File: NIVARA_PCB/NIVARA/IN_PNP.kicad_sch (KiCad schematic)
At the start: 0 parts

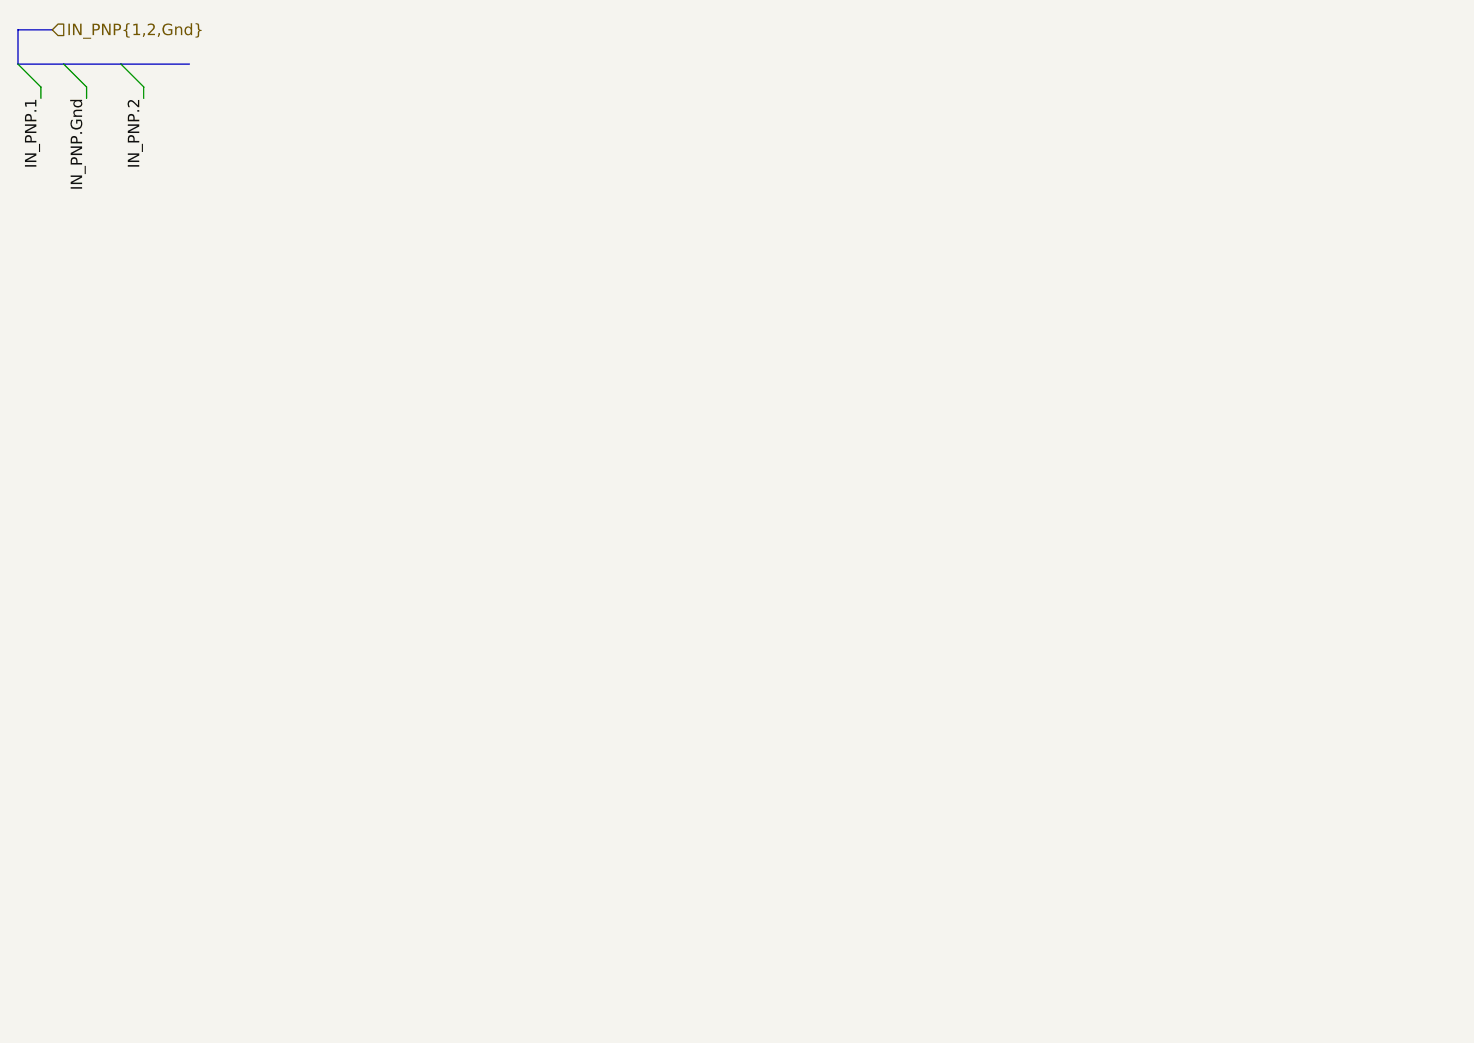
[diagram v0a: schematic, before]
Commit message: AVANCES
se realizaron avances con las entradas NPN, PNP. tambien se realizaron avances con las salidas de RELAYS
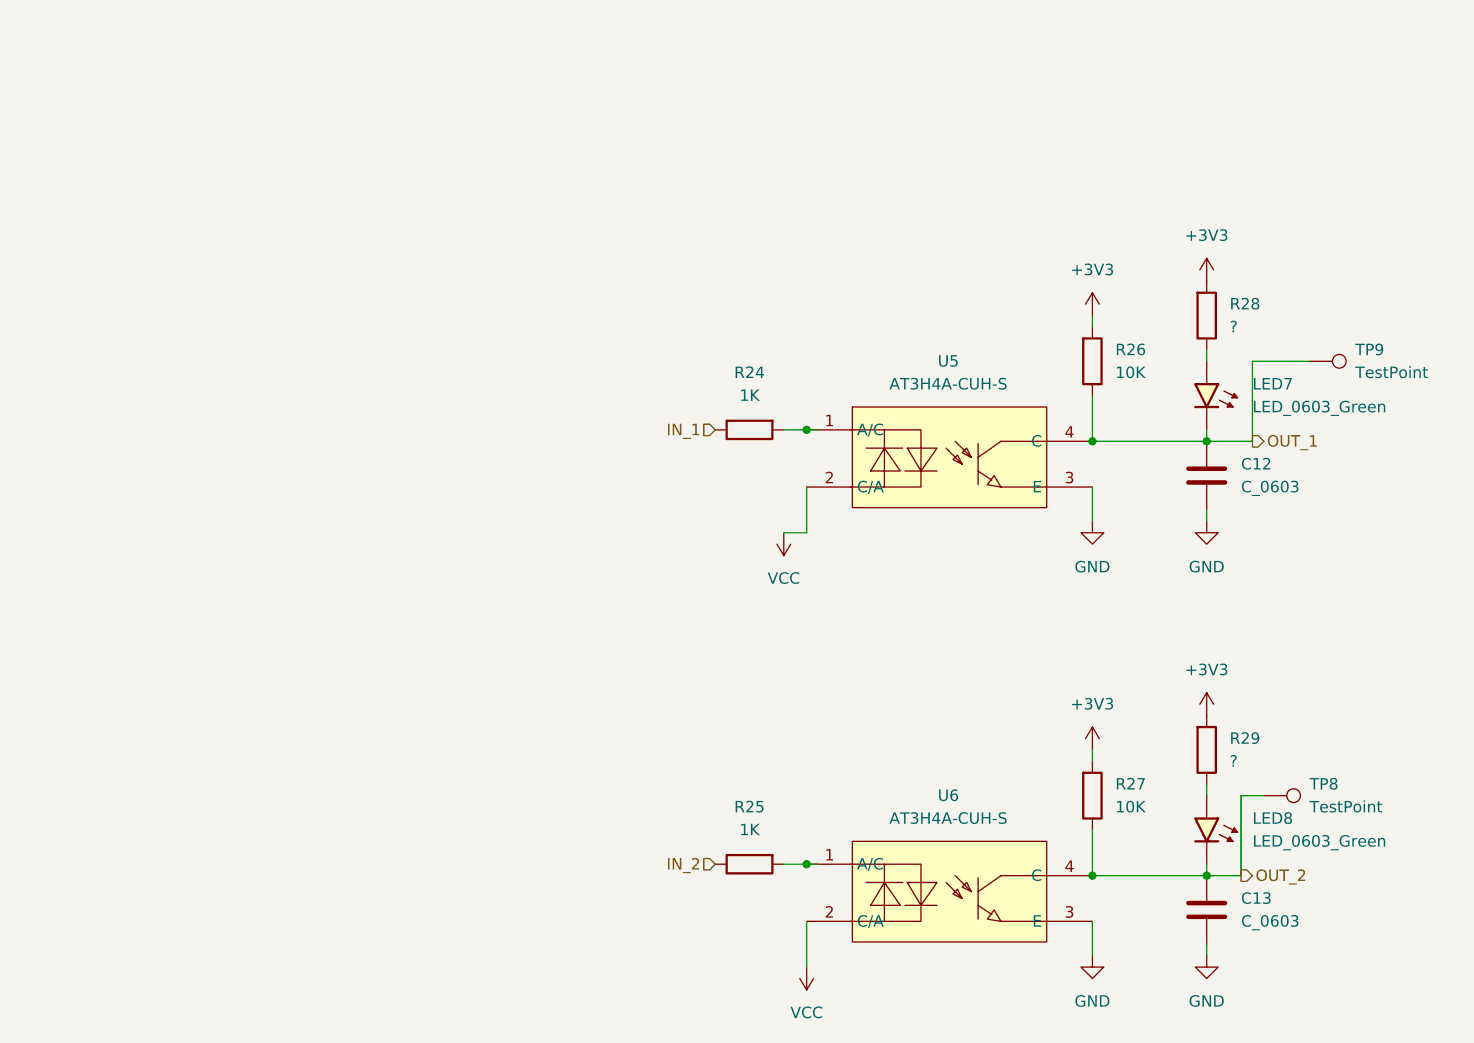
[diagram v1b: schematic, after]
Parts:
- added C12, C13: C_0603, PCM_Capacitor_SMD_AKL:C_0603_1608Metric, symbol PCM_Capacitor_AKL:C_0603
- added LED7, LED8: LED_0603_Green, PCM_LED_SMD_AKL:LED_0603_1608Metric, symbol PCM_LED_AKL:LED_0603_Green
- added R24, R25: 1K, PCM_Resistor_SMD_AKL:R_0603_1608Metric, symbol PCM_Resistor_AKL:R_0603
- added R26, R27: 10K, PCM_Resistor_SMD_AKL:R_0603_1608Metric, symbol PCM_Resistor_AKL:R_0603
- added R28, R29: ?, PCM_Resistor_SMD_AKL:R_0603_1608Metric, symbol PCM_Resistor_AKL:R_0603
- added TP8, TP9: TestPoint, symbol Connector:TestPoint
- added U5, U6: AT3H4A-CUH-S, easyeda2kicad:SSOP-4_L2.7-W4.6-P1.27-LS7.0-TL, symbol easyeda2kicad:AT3H4A-CUH-S
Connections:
- new net: LED7.2 (A), R28.2
- new net: R24.1, U5.1 (A/C)
- new net: LED8.2 (A), R29.2
- new net: R25.1, U6.1 (A/C)
- new net +3V3: R26.1, R27.1, R28.1, R29.1
- new net GND: C12.2, C13.2, U5.3 (E), U6.3 (E)
- new net IN_1: R24.2
- new net IN_2: R25.2
- new net OUT_1: C12.1, LED7.1 (K), R26.2, TP9.1, U5.4 (C)
- new net OUT_2: C13.1, LED8.1 (K), R27.2, TP8.1, U6.4 (C)
- new net VCC: U5.2 (C/A), U6.2 (C/A)

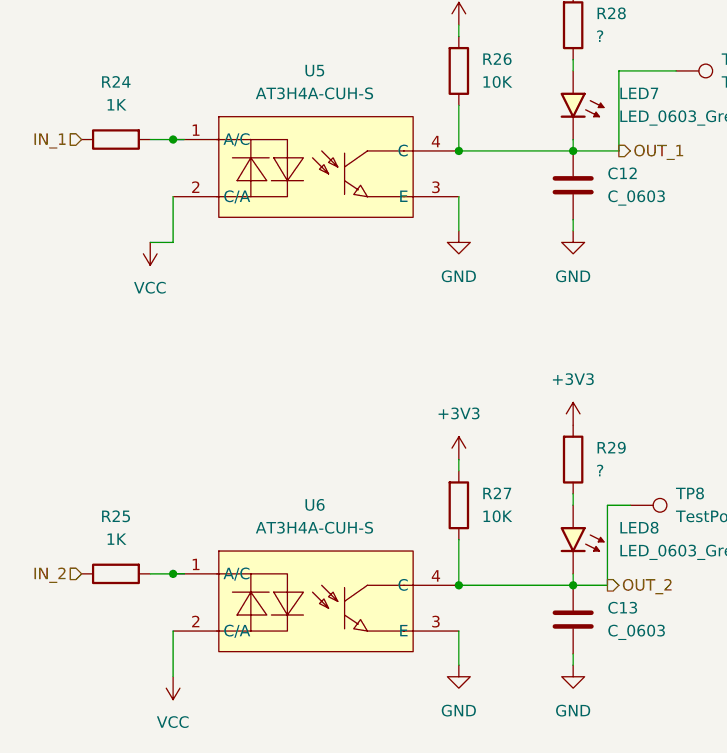
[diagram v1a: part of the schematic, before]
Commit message: se agregaron partnumbers
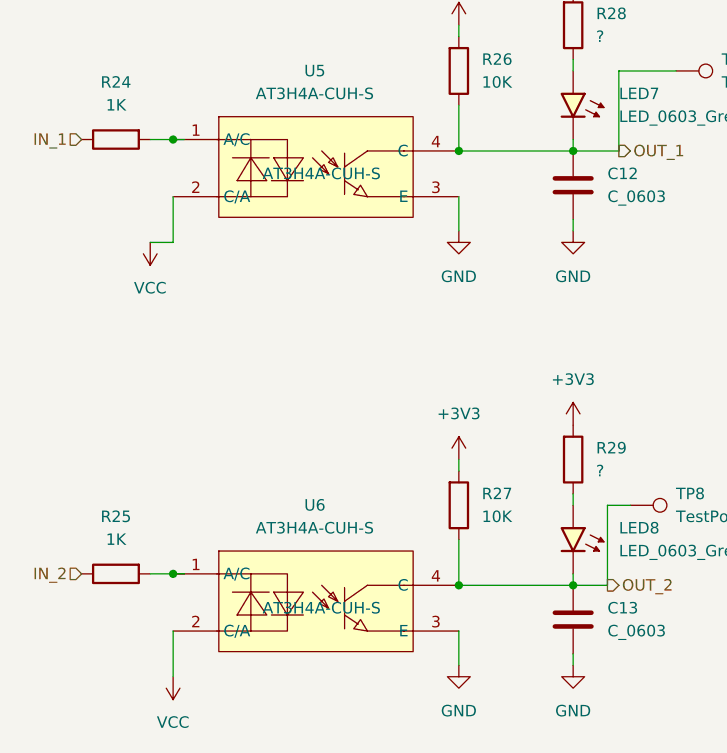
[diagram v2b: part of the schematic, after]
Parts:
- U5, U6: PART NUMBERT (none) -> AT3H4A-CUH-S
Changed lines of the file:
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@@
 			)
 		)
-		(property "PART NUMBERT" ""
+		(property "PART NUMBERT" "AT3H4A-CUH-S"
 			(at 129.54 125.73 0)
 			(effects
@@
 			)
 		)
-		(property "PART NUMBERT" ""
+		(property "PART NUMBERT" "AT3H4A-CUH-S"
 			(at 129.54 77.47 0)
 			(effects

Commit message: RS_485 ADD MODULE
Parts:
- R24, R25: footprint PCM_Resistor_SMD_AKL:R_0603_1608Metric -> PCM_Resistor_SMD_AKL:R_1206_3216Metric_Pad1.30x1.75mm_HandSolder; PART NUMBERT (none) -> CRCW12061K00FKEAHP

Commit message: ACTUALIZACION
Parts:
- TP8, TP9: footprint (none) -> TestPoint:TestPoint_THTPad_D1.0mm_Drill0.5mm
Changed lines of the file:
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@@
 			)
 		)
-		(property "Footprint" ""
+		(property "Footprint" "TestPoint:TestPoint_THTPad_D1.0mm_Drill0.5mm"
 			(at 168.91 71.12 0)
 			(effects
@@
 			)
 		)
-		(property "Footprint" ""
+		(property "Footprint" "TestPoint:TestPoint_THTPad_D1.0mm_Drill0.5mm"
 			(at 163.83 119.38 0)
 			(effects

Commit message: SALIDAS DE VOLTAJE Y CORRIENTE
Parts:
- C12, C13: value C_0603 -> 1uF; PART NUMBERT (none) -> CL10A105KB8NNNC
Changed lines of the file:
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@@
 			)
 		)
-		(property "Value" "C_0603"
+		(property "Value" "1uF"
 			(at 161.29 80.0099 0)
 			(effects
@@
 			)
 		)
-		(property "PART NUMBERT" ""
+		(property "PART NUMBERT" "CL10A105KB8NNNC"
 			(at 157.48 78.74 0)
 			(effects
@@
 			)
 		)
-		(property "Value" "C_0603"
+		(property "Value" "1uF"
 			(at 161.29 128.2699 0)
 			(effects
@@
 			)
 		)
-		(property "PART NUMBERT" ""
+		(property "PART NUMBERT" "CL10A105KB8NNNC"
 			(at 157.48 127 0)
 			(effects

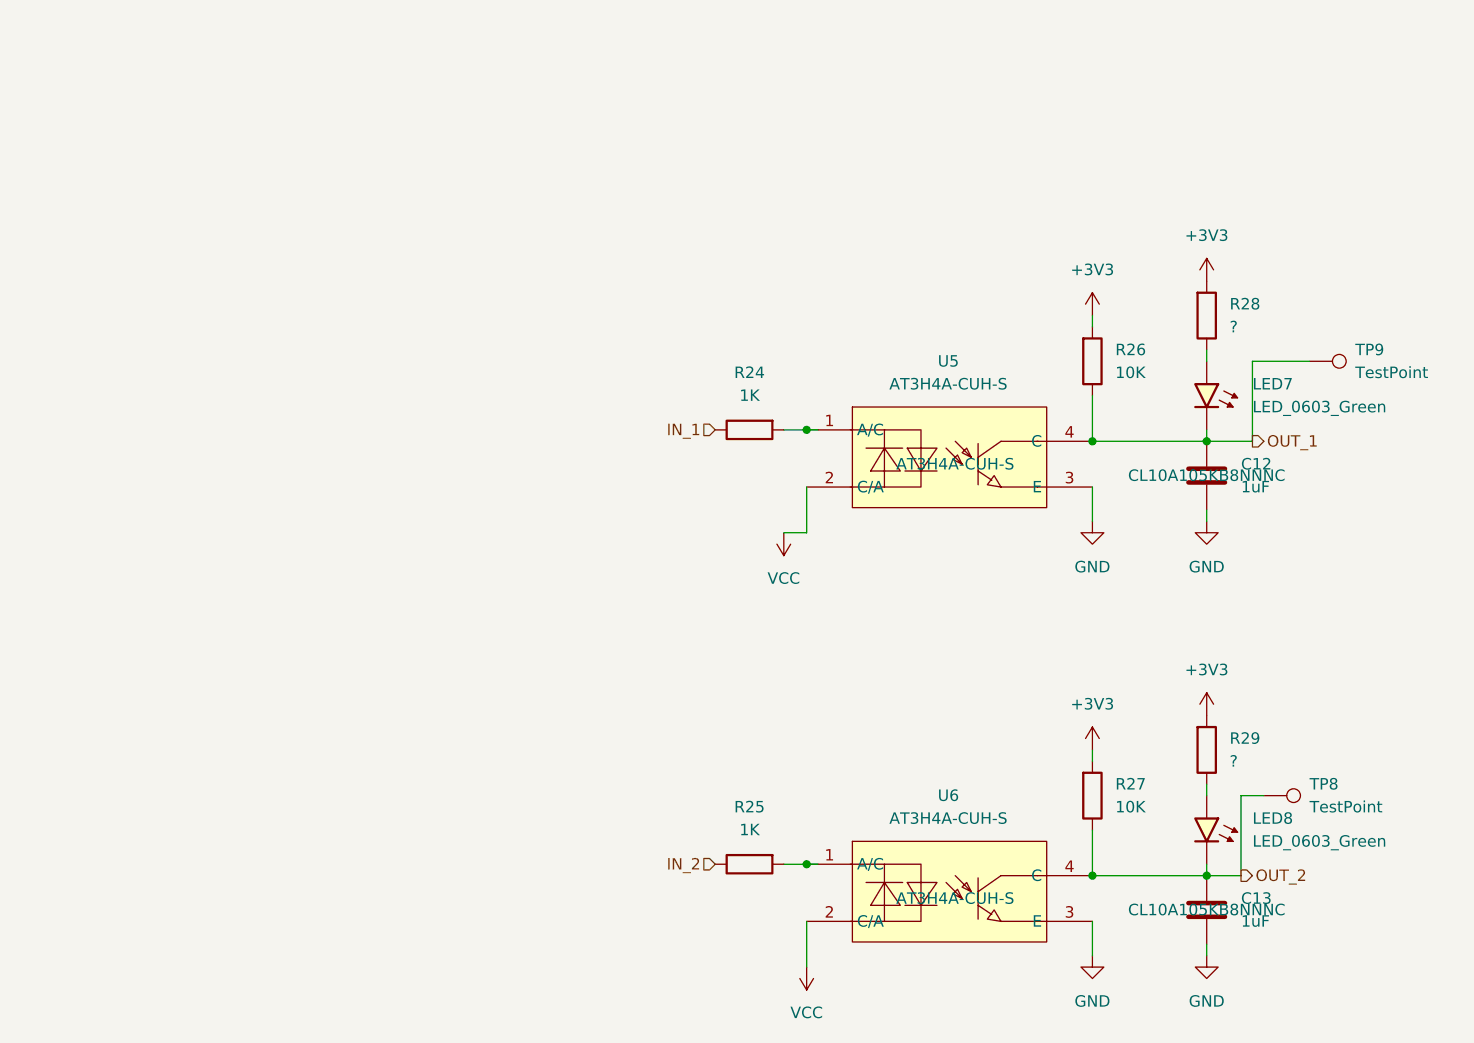
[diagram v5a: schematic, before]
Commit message: Se organizaron componentes en el area de PCB
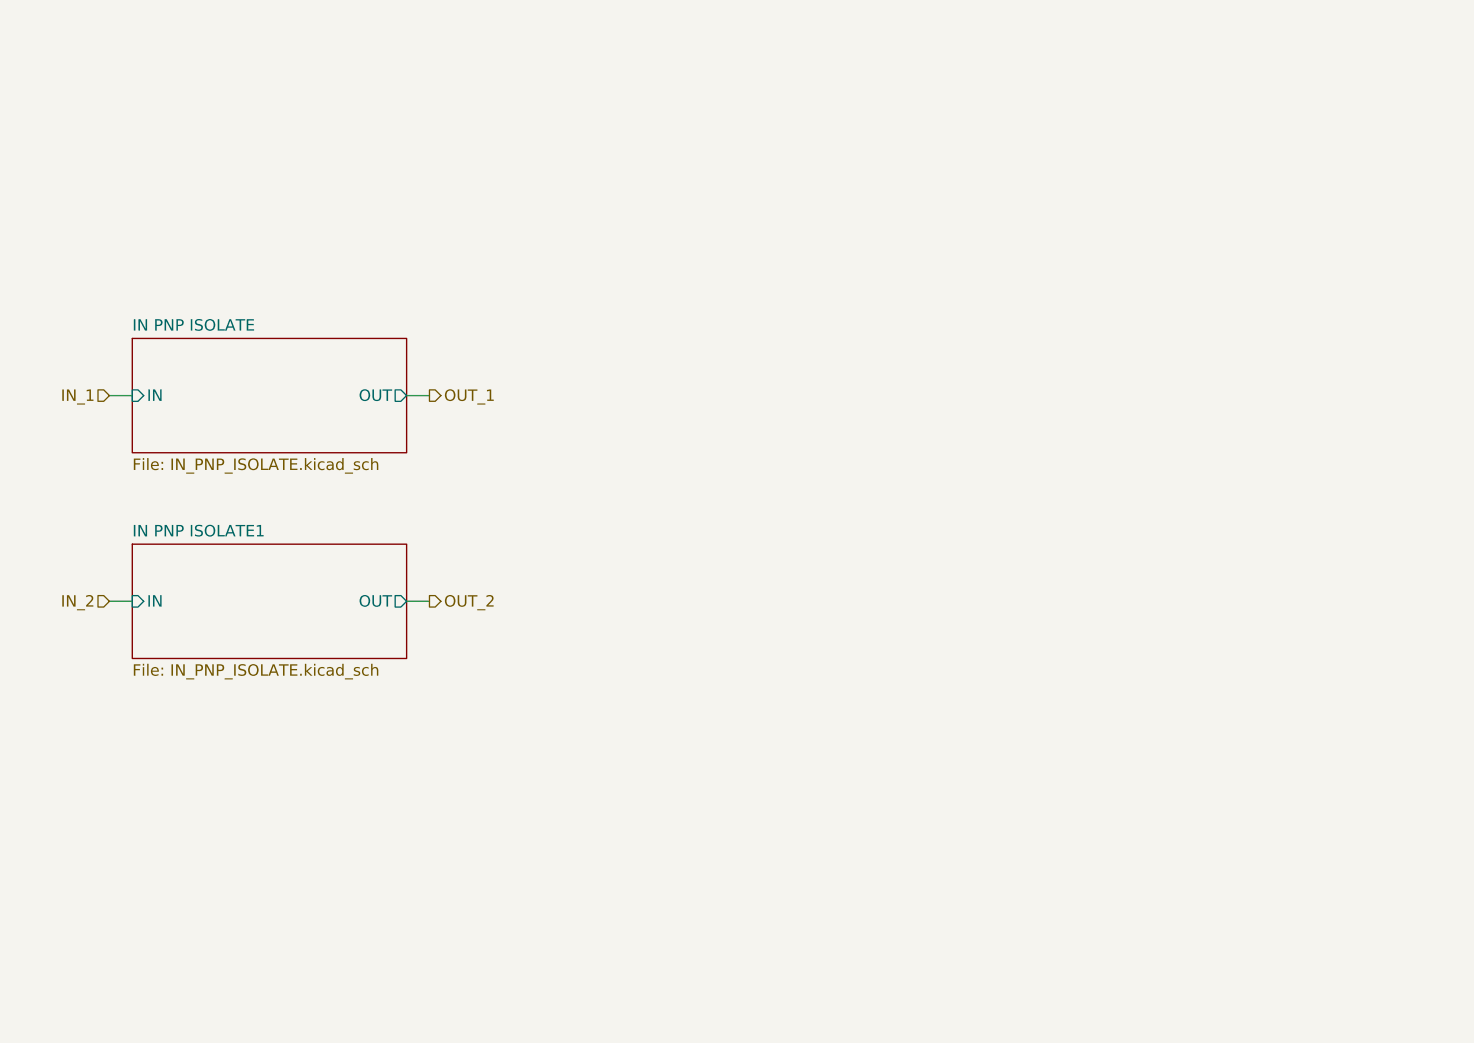
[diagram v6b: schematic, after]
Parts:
- removed C12, C13: 1uF, PCM_Capacitor_SMD_AKL:C_0603_1608Metric, symbol PCM_Capacitor_AKL:C_0603
- removed LED7, LED8: LED_0603_Green, PCM_LED_SMD_AKL:LED_0603_1608Metric, symbol PCM_LED_AKL:LED_0603_Green
- removed R24, R25: 1K, PCM_Resistor_SMD_AKL:R_1206_3216Metric_Pad1.30x1.75mm_HandSolder, symbol PCM_Resistor_AKL:R_0603
- removed R26, R27: 10K, PCM_Resistor_SMD_AKL:R_0603_1608Metric, symbol PCM_Resistor_AKL:R_0603
- removed R28, R29: ?, PCM_Resistor_SMD_AKL:R_0603_1608Metric, symbol PCM_Resistor_AKL:R_0603
- removed TP8, TP9: TestPoint, TestPoint:TestPoint_THTPad_D1.0mm_Drill0.5mm, symbol Connector:TestPoint
- removed U5, U6: AT3H4A-CUH-S, easyeda2kicad:SSOP-4_L2.7-W4.6-P1.27-LS7.0-TL, symbol easyeda2kicad:AT3H4A-CUH-S
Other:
- added sheet IN PNP ISOLATE (IN_PNP_ISOLATE.kicad_sch)
- added sheet IN PNP ISOLATE1 (IN_PNP_ISOLATE.kicad_sch)
